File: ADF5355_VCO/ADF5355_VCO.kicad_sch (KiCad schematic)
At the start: 0 parts

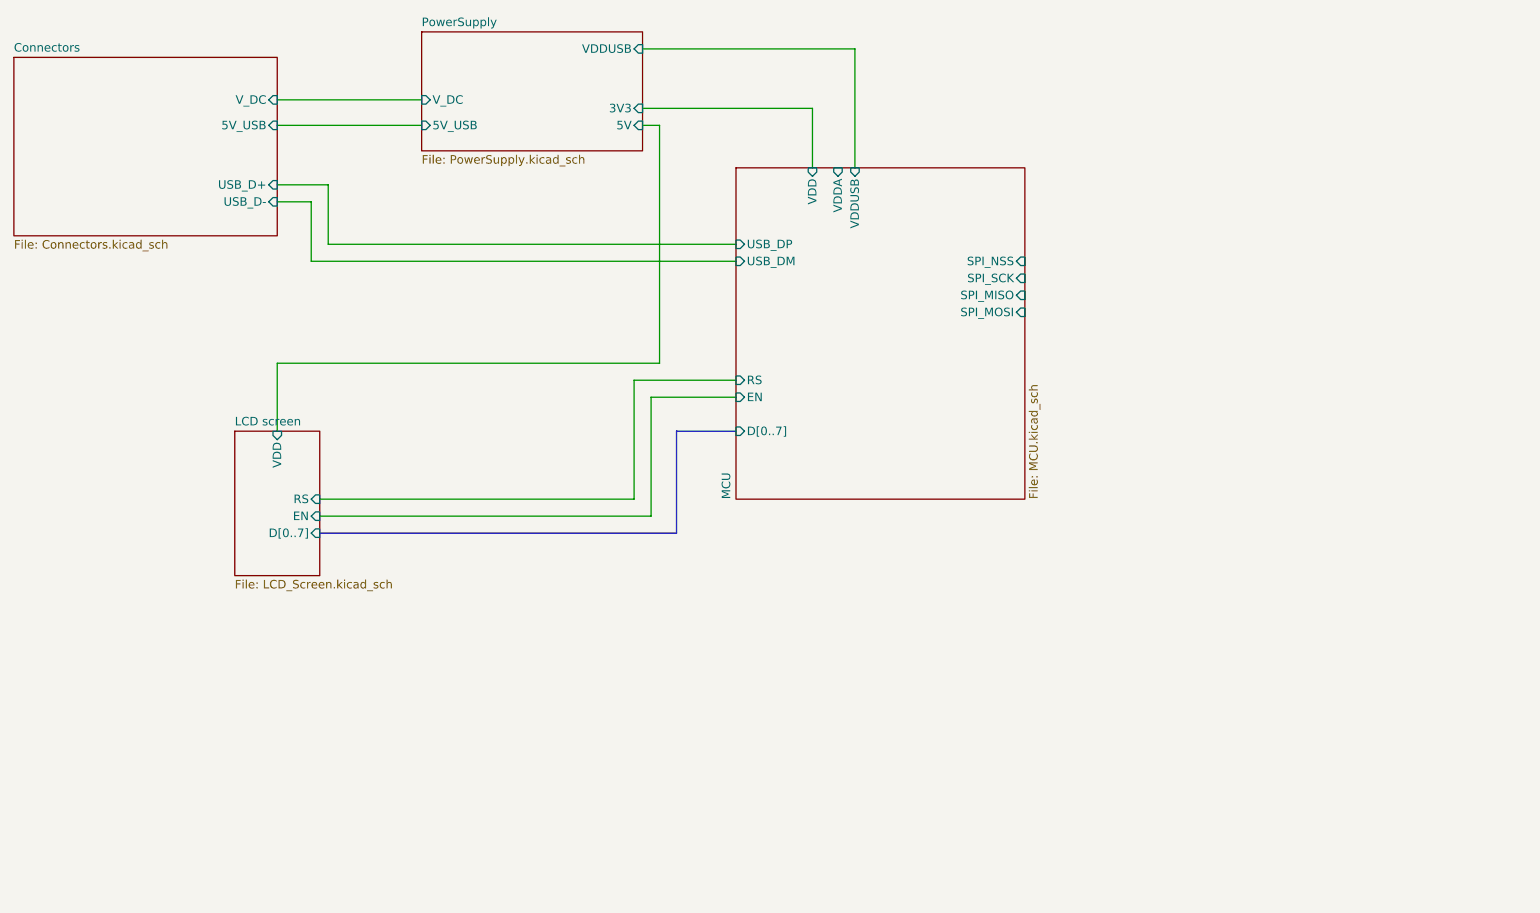
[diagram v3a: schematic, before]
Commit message: Added ADF5355 to the schematic
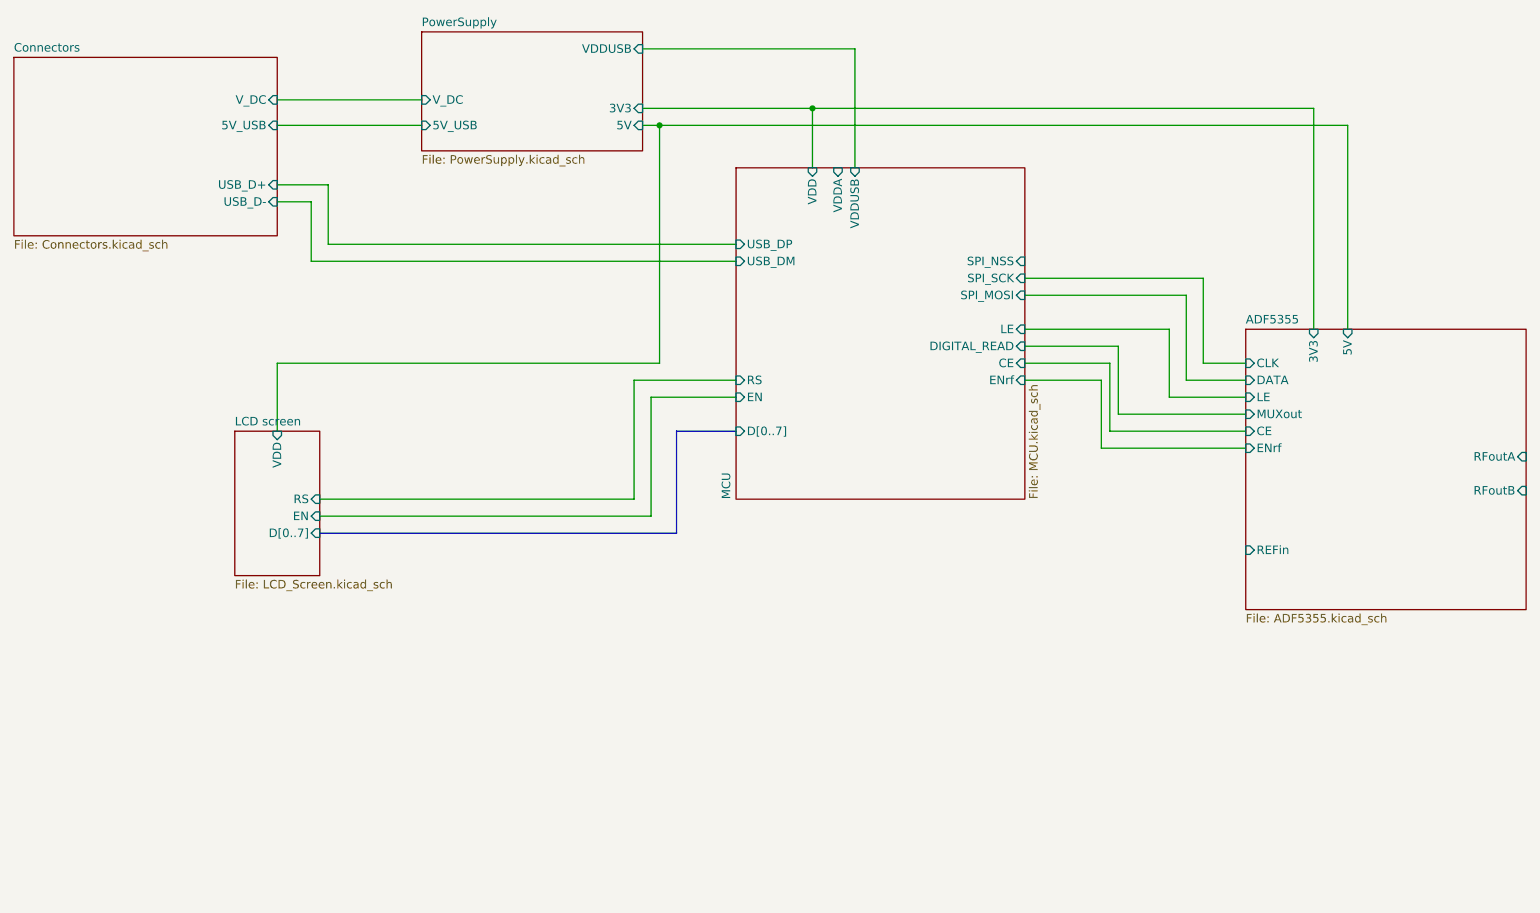
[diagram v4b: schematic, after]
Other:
- added sheet ADF5355 (ADF5355.kicad_sch)
- sheet MCU ports: added CE, DIGITAL_READ, ENrf, LE; removed SPI_MISO
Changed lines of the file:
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@@
 (kicad_sch (version 20230121) (generator eeschema)
   (paper "A4")
+  (junction (at 116.84 38.1) (diameter 0) (color 0 0 0 0)
+  )
+  (junction (at 139.7 35.56) (diameter 0) (color 0 0 0 0)
+  )
   (wire (pts (xy 66.04 96.52) (xy 115.57 96.52))
     (stroke (width 0) (type default))
   )
+  (wire (pts (xy 193.04 78.74) (xy 204.47 78.74))
+    (stroke (width 0) (type default))
+  )
   (wire (pts (xy 59.69 49.53) (xy 64.77 49.53))
     (stroke (width 0) (type default))
   )
+  (wire (pts (xy 185.42 81.28) (xy 204.47 81.28))
+    (stroke (width 0) (type default))
+  )
   (wire (pts (xy 115.57 78.74) (xy 115.57 96.52))
     (stroke (width 0) (type default))
   )
+  (wire (pts (xy 182.88 76.2) (xy 182.88 86.36))
+    (stroke (width 0) (type default))
+  )
   (wire (pts (xy 64.77 49.53) (xy 64.77 58.42))
     (stroke (width 0) (type default))
@@
     (stroke (width 0) (type default))
   )
+  (wire (pts (xy 195.58 63.5) (xy 195.58 76.2))
+    (stroke (width 0) (type default))
+  )
   (wire (pts (xy 114.3 38.1) (xy 116.84 38.1))
     (stroke (width 0) (type default))
   )
+  (wire (pts (xy 214.63 35.56) (xy 139.7 35.56))
+    (stroke (width 0) (type default))
+  )
   (wire (pts (xy 64.77 58.42) (xy 128.27 58.42))
     (stroke (width 0) (type default))
   )
+  (wire (pts (xy 184.15 73.66) (xy 184.15 83.82))
+    (stroke (width 0) (type default))
+  )
   (wire (pts (xy 114.3 26.67) (xy 146.05 26.67))
     (stroke (width 0) (type default))
   )
+  (wire (pts (xy 185.42 71.12) (xy 185.42 81.28))
+    (stroke (width 0) (type default))
+  )
   (wire (pts (xy 67.31 55.88) (xy 128.27 55.88))
     (stroke (width 0) (type default))
   )
+  (wire (pts (xy 171.45 73.66) (xy 184.15 73.66))
+    (stroke (width 0) (type default))
+  )
+  (wire (pts (xy 171.45 71.12) (xy 185.42 71.12))
+    (stroke (width 0) (type default))
+  )
+  (wire (pts (xy 184.15 83.82) (xy 204.47 83.82))
+    (stroke (width 0) (type default))
+  )
   (wire (pts (xy 59.69 46.99) (xy 67.31 46.99))
     (stroke (width 0) (type default))
   )
+  (wire (pts (xy 171.45 76.2) (xy 182.88 76.2))
+    (stroke (width 0) (type default))
+  )
   (wire (pts (xy 113.03 76.2) (xy 113.03 93.98))
     (stroke (width 0) (type default))
   )
+  (wire (pts (xy 198.12 73.66) (xy 198.12 60.96))
+    (stroke (width 0) (type default))
+  )
+  (wire (pts (xy 116.84 38.1) (xy 219.71 38.1))
+    (stroke (width 0) (type default))
+  )
   (wire (pts (xy 116.84 38.1) (xy 116.84 73.66))
     (stroke (width 0) (type default))
@@
     (stroke (width 0) (type default))
   )
+  (wire (pts (xy 171.45 68.58) (xy 193.04 68.58))
+    (stroke (width 0) (type default))
+  )
+  (wire (pts (xy 214.63 68.58) (xy 214.63 35.56))
+    (stroke (width 0) (type default))
+  )
   (wire (pts (xy 128.27 78.74) (xy 115.57 78.74))
     (stroke (width 0) (type default))
   )
+  (wire (pts (xy 182.88 86.36) (xy 204.47 86.36))
+    (stroke (width 0) (type default))
+  )
   (wire (pts (xy 59.69 34.29) (xy 81.28 34.29))
     (stroke (width 0) (type default))
@@
     (stroke (width 0) (type default))
   )
+  (wire (pts (xy 171.45 63.5) (xy 195.58 63.5))
+    (stroke (width 0) (type default))
+  )
   (wire (pts (xy 59.69 73.66) (xy 59.69 83.82))
     (stroke (width 0) (type default))
   )
+  (wire (pts (xy 195.58 76.2) (xy 204.47 76.2))
+    (stroke (width 0) (type default))
+  )
   (wire (pts (xy 128.27 76.2) (xy 113.03 76.2))
     (stroke (width 0) (type default))
   )
+  (wire (pts (xy 198.12 73.66) (xy 204.47 73.66))
+    (stroke (width 0) (type default))
+  )
   (bus (pts (xy 128.27 83.82) (xy 119.38 83.82))
     (stroke (width 0) (type default))
   )
+  (wire (pts (xy 219.71 38.1) (xy 219.71 68.58))
+    (stroke (width 0) (type default))
+  )
+  (wire (pts (xy 193.04 68.58) (xy 193.04 78.74))
+    (stroke (width 0) (type default))
+  )
   (bus (pts (xy 66.04 99.06) (xy 119.38 99.06))
+    (stroke (width 0) (type default))
+  )
+  (wire (pts (xy 171.45 60.96) (xy 198.12 60.96))
     (stroke (width 0) (type default))
   )
@@
       (effects (font (size 1.27 1.27)) (justify left))
     )
-    (pin "SPI_MISO" input (at 171.45 63.5 0)
-      (effects (font (size 1.27 1.27)) (justify right))
-    )
     (pin "SPI_NSS" input (at 171.45 58.42 0)
       (effects (font (size 1.27 1.27)) (justify right))
@@
       (effects (font (size 1.27 1.27)) (justify right))
     )
-    (pin "SPI_MOSI" input (at 171.45 66.04 0)
+    (pin "SPI_MOSI" input (at 171.45 63.5 0)
       (effects (font (size 1.27 1.27)) (justify right))
     )
@@
     (pin "EN" input (at 128.27 78.74 180)
       (effects (font (size 1.27 1.27)) (justify left))
+    )
+    (pin "DIGITAL_READ" input (at 171.45 71.12 0)
+      (effects (font (size 1.27 1.27)) (justify right))
+    )
+    (pin "LE" input (at 171.45 68.58 0)
+      (effects (font (size 1.27 1.27)) (justify right))
+    )
+    (pin "CE" input (at 171.45 73.66 0)
+      (effects (font (size 1.27 1.27)) (justify right))
+    )
+    (pin "ENrf" input (at 171.45 76.2 0)
+      (effects (font (size 1.27 1.27)) (justify right))
     )
     (instances
@@
       )
     )
+  )
+  (sheet (at 204.47 68.58) (size 41.91 41.91) (fields_autoplaced)
+    (stroke (width 0.1524) (type solid))
+    (fill (color 255 240 101 1.0000))
+    (property "Sheetname" "ADF5355" (at 204.47 67.8684 0)
+      (effects (font (size 1.27 1.27)) (justify left bottom))
+    )
+    (property "Sheetfile" "ADF5355.kicad_sch" (at 204.47 111.0746 0)
+      (effects (font (size 1.27 1.27)) (justify left top))
+    )
+    (pin "3V3" input (at 214.63 68.58 90)
+      (effects (font (size 1.27 1.27)) (justify right))
+    )
+    (pin "5V" input (at 219.71 68.58 90)
+      (effects (font (size 1.27 1.27)) (justify right))
+    )
+    (pin "ENrf" input (at 204.47 86.36 180)
+      (effects (font (size 1.27 1.27)) (justify left))
+    )
+    (pin "CE" input (at 204.47 83.82 180)
+      (effects (font (size 1.27 1.27)) (justify left))
+    )
+    (pin "MUXout" input (at 204.47 81.28 180)
+      (effects (font (size 1.27 1.27)) (justify left))
+    )
+    (pin "LE" input (at 204.47 78.74 180)
+      (effects (font (size 1.27 1.27)) (justify left))
+    )
+    (pin "DATA" input (at 204.47 76.2 180)
+      (effects (font (size 1.27 1.27)) (justify left))
+    )
+    (pin "CLK" input (at 204.47 73.66 180)
+      (effects (font (size 1.27 1.27)) (justify left))
+    )
+    (pin "REFin" input (at 204.47 101.6 180)
+      (effects (font (size 1.27 1.27)) (justify left))
+    )
+    (pin "RFoutB" input (at 246.38 92.71 0)
+      (effects (font (size 1.27 1.27)) (justify right))
+    )
+    (pin "RFoutA" input (at 246.38 87.63 0)
+      (effects (font (size 1.27 1.27)) (justify right))
+    )
+    (instances
+      (project "ADF5355_VCO"
+        (path "/29349b68-071c-451b-9b1e-10b5ef7e12a6" (page "6"))
+      )
+    )

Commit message: Changed the power port
Changed all power ports to be global instead of them being hierarchical sheet pins
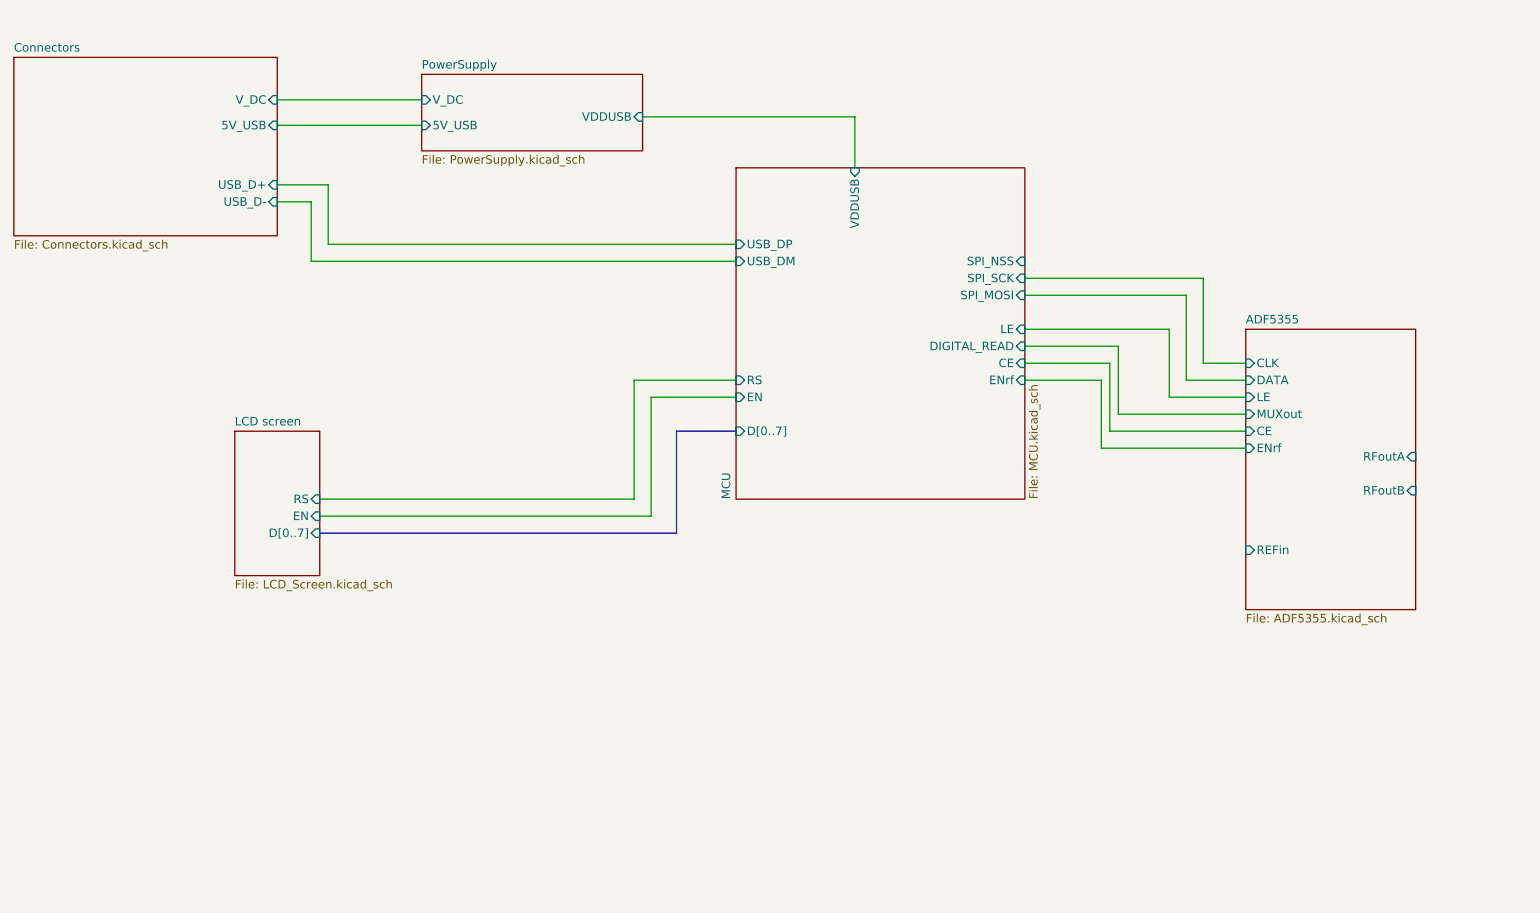
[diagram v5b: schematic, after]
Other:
- sheet ADF5355 ports: added none; removed 3V3, 5V
- sheet LCD screen ports: added none; removed VDD
- sheet MCU ports: added none; removed VDD, VDDA
- sheet PowerSupply ports: added none; removed 3V3, 5V
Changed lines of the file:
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@@
 (kicad_sch (version 20230121) (generator eeschema)
   (paper "A4")
-  (junction (at 116.84 38.1) (diameter 0) (color 0 0 0 0)
-  )
-  (junction (at 139.7 35.56) (diameter 0) (color 0 0 0 0)
-  )
   (wire (pts (xy 66.04 96.52) (xy 115.57 96.52))
     (stroke (width 0) (type default))
@@
     (stroke (width 0) (type default))
   )
-  (wire (pts (xy 59.69 73.66) (xy 116.84 73.66))
-    (stroke (width 0) (type default))
-  )
   (wire (pts (xy 66.04 93.98) (xy 113.03 93.98))
     (stroke (width 0) (type default))
@@
     (stroke (width 0) (type default))
   )
-  (wire (pts (xy 114.3 38.1) (xy 116.84 38.1))
-    (stroke (width 0) (type default))
-  )
-  (wire (pts (xy 214.63 35.56) (xy 139.7 35.56))
-    (stroke (width 0) (type default))
-  )
   (wire (pts (xy 64.77 58.42) (xy 128.27 58.42))
     (stroke (width 0) (type default))
@@
     (stroke (width 0) (type default))
   )
-  (wire (pts (xy 114.3 26.67) (xy 146.05 26.67))
+  (wire (pts (xy 114.3 36.83) (xy 146.05 36.83))
     (stroke (width 0) (type default))
   )
@@
     (stroke (width 0) (type default))
   )
-  (wire (pts (xy 116.84 38.1) (xy 219.71 38.1))
-    (stroke (width 0) (type default))
-  )
-  (wire (pts (xy 116.84 38.1) (xy 116.84 73.66))
-    (stroke (width 0) (type default))
-  )
   (bus (pts (xy 119.38 83.82) (xy 119.38 99.06))
     (stroke (width 0) (type default))
@@
     (stroke (width 0) (type default))
   )
-  (wire (pts (xy 214.63 68.58) (xy 214.63 35.56))
-    (stroke (width 0) (type default))
-  )
   (wire (pts (xy 128.27 78.74) (xy 115.57 78.74))
     (stroke (width 0) (type default))
@@
     (stroke (width 0) (type default))
   )
-  (wire (pts (xy 139.7 35.56) (xy 139.7 44.45))
-    (stroke (width 0) (type default))
-  )
-  (wire (pts (xy 114.3 35.56) (xy 139.7 35.56))
-    (stroke (width 0) (type default))
-  )
   (wire (pts (xy 171.45 63.5) (xy 195.58 63.5))
     (stroke (width 0) (type default))
   )
-  (wire (pts (xy 59.69 73.66) (xy 59.69 83.82))
-    (stroke (width 0) (type default))
-  )
   (wire (pts (xy 195.58 76.2) (xy 204.47 76.2))
     (stroke (width 0) (type default))
@@
     (stroke (width 0) (type default))
   )
-  (wire (pts (xy 219.71 38.1) (xy 219.71 68.58))
-    (stroke (width 0) (type default))
-  )
   (wire (pts (xy 193.04 68.58) (xy 193.04 78.74))
     (stroke (width 0) (type default))
@@
     (stroke (width 0) (type default))
   )
-  (wire (pts (xy 146.05 26.67) (xy 146.05 44.45))
+  (wire (pts (xy 146.05 36.83) (xy 146.05 44.45))
     (stroke (width 0) (type default))
   )
@@
     (stroke (width 0) (type default))
   )
-  (sheet (at 81.28 24.13) (size 33.02 17.78) (fields_autoplaced)
+  (sheet (at 81.28 30.48) (size 33.02 11.43) (fields_autoplaced)
     (stroke (width 0) (type solid))
     (fill (color 255 240 101 1.0000))
-    (property "Sheetname" "PowerSupply" (at 81.28 23.4184 0)
+    (property "Sheetname" "PowerSupply" (at 81.28 29.7684 0)
       (effects (font (size 1.27 1.27)) (justify left bottom))
     )
@@
       (effects (font (size 1.27 1.27)) (justify left top))
     )
-    (pin "3V3" input (at 114.3 35.56 0)
-      (effects (font (size 1.27 1.27)) (justify right))
-    )
-    (pin "5V" input (at 114.3 38.1 0)
-      (effects (font (size 1.27 1.27)) (justify right))
-    )
     (pin "V_DC" input (at 81.28 34.29 180)
       (effects (font (size 1.27 1.27)) (justify left))
@@
       (effects (font (size 1.27 1.27)) (justify left))
     )
-    (pin "VDDUSB" input (at 114.3 26.67 0)
+    (pin "VDDUSB" input (at 114.3 36.83 0)
       (effects (font (size 1.27 1.27)) (justify right))
     )
@@
       (effects (font (size 1.27 1.27)) (justify left top))
     )
-    (pin "VDD" input (at 139.7 44.45 90)
-      (effects (font (size 1.27 1.27)) (justify right))
-    )
     (pin "VDDUSB" input (at 146.05 44.45 90)
-      (effects (font (size 1.27 1.27)) (justify right))
-    )
-    (pin "VDDA" input (at 143.51 44.45 90)
       (effects (font (size 1.27 1.27)) (justify right))
     )
@@
     )
   )
-  (sheet (at 204.47 68.58) (size 41.91 41.91) (fields_autoplaced)
+  (sheet (at 204.47 68.58) (size 25.4 41.91) (fields_autoplaced)
     (stroke (width 0.1524) (type solid))
     (fill (color 255 240 101 1.0000))
@@
       (effects (font (size 1.27 1.27)) (justify left top))
     )
-    (pin "3V3" input (at 214.63 68.58 90)
-      (effects (font (size 1.27 1.27)) (justify right))
-    )
-    (pin "5V" input (at 219.71 68.58 90)
-      (effects (font (size 1.27 1.27)) (justify right))
-    )
     (pin "ENrf" input (at 204.47 86.36 180)
       (effects (font (size 1.27 1.27)) (justify left))
@@
       (effects (font (size 1.27 1.27)) (justify left))
     )
-    (pin "RFoutB" input (at 246.38 92.71 0)
-      (effects (font (size 1.27 1.27)) (justify right))
-    )
-    (pin "RFoutA" input (at 246.38 87.63 0)
+    (pin "RFoutB" input (at 229.87 92.71 0)
+      (effects (font (size 1.27 1.27)) (justify right))
+    )
+    (pin "RFoutA" input (at 229.87 87.63 0)
       (effects (font (size 1.27 1.27)) (justify right))
     )
@@
       (effects (font (size 1.27 1.27)) (justify right))
     )
-    (pin "VDD" input (at 59.69 83.82 90)
-      (effects (font (size 1.27 1.27)) (justify right))
-    )
